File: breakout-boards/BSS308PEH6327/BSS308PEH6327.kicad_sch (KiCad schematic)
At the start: 0 parts

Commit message: feat: add capacitor breakout board
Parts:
- added J1, J2, J3: Conn_01x12, Connector_PinSocket_2.54mm:PinSocket_1x12_P2.54mm_Vertical, symbol Connector_Generic:Conn_01x12
- added Q1, Q10, Q11, Q12, Q2, Q3, Q4, Q5, Q6, Q7, Q8, Q9: BSS308PE_H6327, SOT95P260X110-3N, symbol FixedWing:BSS308PE_H6327
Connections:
- new net: J2.1 (Pin_1), Q1.3 (D)
- new net: J2.10 (Pin_10), Q10.3 (D)
- new net: J2.11 (Pin_11), Q11.3 (D)
- new net: J2.12 (Pin_12), Q12.3 (D)
- new net: J2.2 (Pin_2), Q2.3 (D)
- new net: J2.3 (Pin_3), Q3.3 (D)
- new net: J2.4 (Pin_4), Q4.3 (D)
- new net: J2.5 (Pin_5), Q5.3 (D)
- new net: J2.6 (Pin_6), Q6.3 (D)
- new net: J2.7 (Pin_7), Q7.3 (D)
- new net: J2.8 (Pin_8), Q8.3 (D)
- new net: J2.9 (Pin_9), Q9.3 (D)
- new net: J1.12 (Pin_12), Q12.1 (G)
- new net: J3.12 (Pin_12), Q12.2 (S)
- new net: J1.9 (Pin_9), Q9.1 (G)
- new net: J3.9 (Pin_9), Q9.2 (S)
- new net: J1.7 (Pin_7), Q7.1 (G)
- new net: J3.7 (Pin_7), Q7.2 (S)
- new net: J1.4 (Pin_4), Q4.1 (G)
- new net: J3.4 (Pin_4), Q4.2 (S)
- new net: J1.5 (Pin_5), Q5.1 (G)
- new net: J3.5 (Pin_5), Q5.2 (S)
- new net: J1.8 (Pin_8), Q8.1 (G)
- new net: J3.8 (Pin_8), Q8.2 (S)
- new net: J3.1 (Pin_1), Q1.2 (S)
- new net: J3.10 (Pin_10), Q10.2 (S)
- new net: J3.11 (Pin_11), Q11.2 (S)
- new net: J3.2 (Pin_2), Q2.2 (S)
- new net: J3.3 (Pin_3), Q3.2 (S)
- new net: J3.6 (Pin_6), Q6.2 (S)
- new net: J1.1 (Pin_1), Q1.1 (G)
- new net: J1.10 (Pin_10), Q10.1 (G)
- new net: J1.11 (Pin_11), Q11.1 (G)
- new net: J1.2 (Pin_2), Q2.1 (G)
- new net: J1.3 (Pin_3), Q3.1 (G)
- new net: J1.6 (Pin_6), Q6.1 (G)

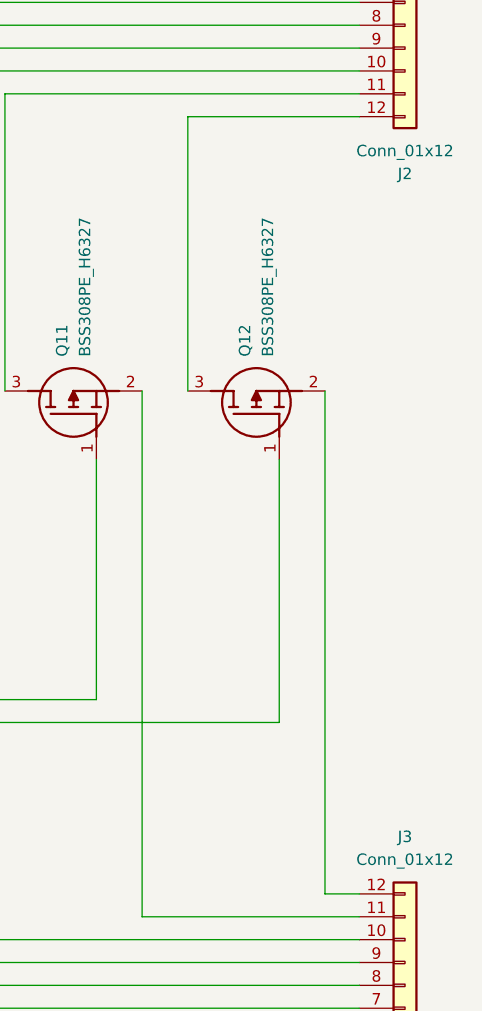
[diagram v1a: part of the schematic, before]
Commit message: feat: update MOSFET pcb and schem
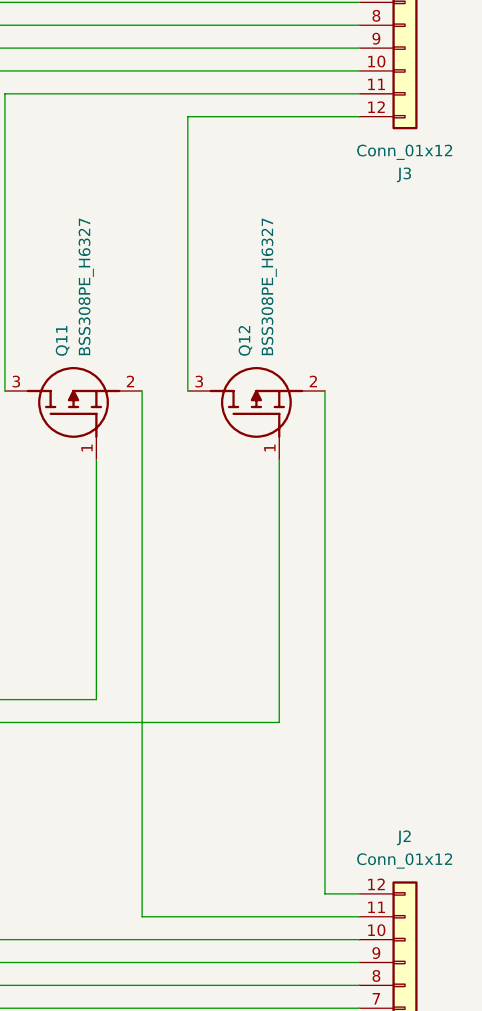
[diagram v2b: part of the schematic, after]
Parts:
- renumbered J3 to J2, J2 to J3
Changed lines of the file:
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@@
   (symbol (lib_id "Connector_Generic:Conn_01x12") (at 273.05 36.83 0) (unit 1)
     (in_bom yes) (on_board yes) (dnp no)
-    (property "Reference" "J2" (at 273.05 58.42 0)
+    (property "Reference" "J3" (at 273.05 58.42 0)
       (effects (font (size 1.27 1.27)))
     )
@@
       (project "BSS308PEH6327"
         (path "/8fa9ade4-ce80-4c27-9e96-ce2c5051f917"
-          (reference "J2") (unit 1)
+          (reference "J3") (unit 1)
         )
       )
@@
   (symbol (lib_id "Connector_Generic:Conn_01x12") (at 273.05 153.67 0) (mirror x) (unit 1)
     (in_bom yes) (on_board yes) (dnp no)
-    (property "Reference" "J3" (at 273.05 132.08 0)
+    (property "Reference" "J2" (at 273.05 132.08 0)
       (effects (font (size 1.27 1.27)))
     )
@@
       (project "BSS308PEH6327"
         (path "/8fa9ade4-ce80-4c27-9e96-ce2c5051f917"
-          (reference "J3") (unit 1)
-        )
-      )
+          (reference "J2") (unit 1)
+        )
+      )
